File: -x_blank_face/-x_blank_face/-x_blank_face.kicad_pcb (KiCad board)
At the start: 2 copper layers, 87 x 326.5 mm, 29 parts, among them J1 Conn_01x08_Pin, J2 Conn_01x02_Pin, J3 Conn_01x02_Pin

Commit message: Rerouted some stuff
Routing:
- net GND: track 221.4 -> 216.8 mm
- net /-X Serial Out: track 219.9 -> 215.8 mm

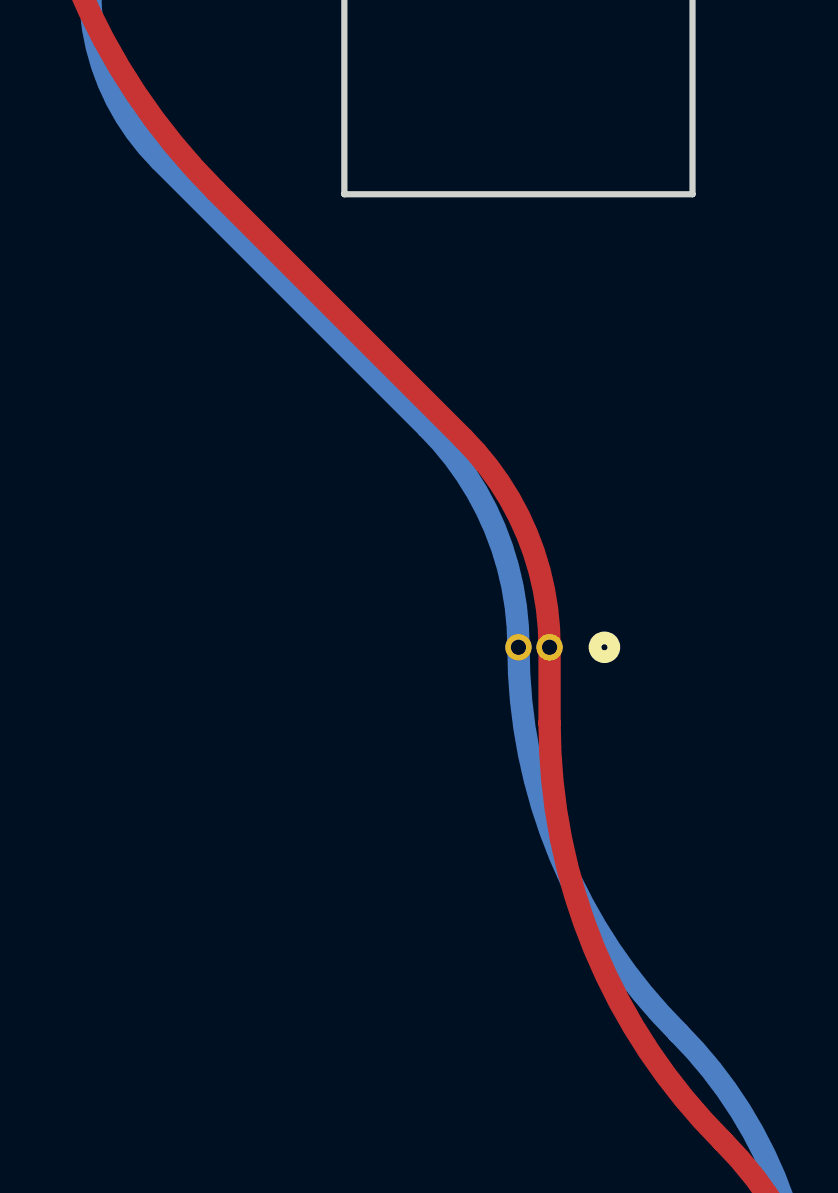
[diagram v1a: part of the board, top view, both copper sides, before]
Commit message: removed solder mask from footprint
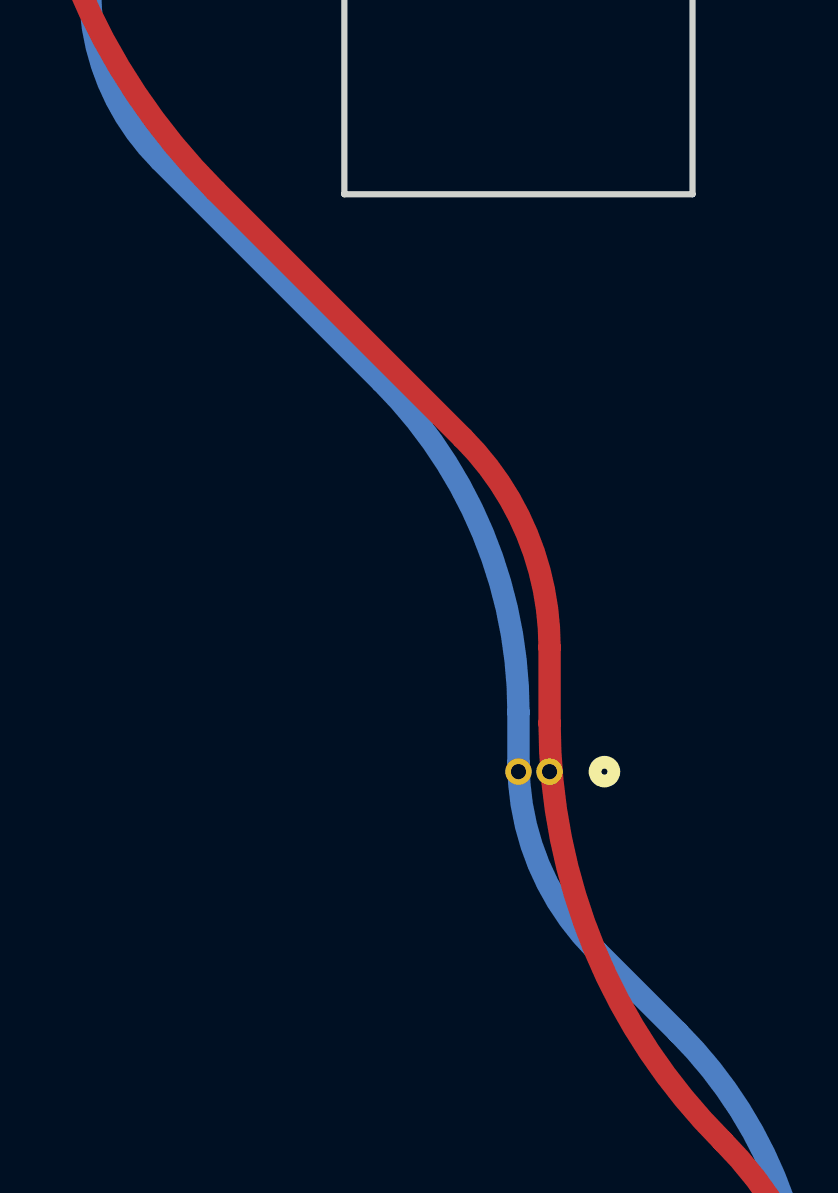
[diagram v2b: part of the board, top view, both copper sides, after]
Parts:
- moved J2 5.00 mm to (134.8, 25.6)
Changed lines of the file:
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@@
 	(footprint "CNN_GNSS_Footprint:CON2_1X2_UR_DF13"
 		(layer "B.Cu")
-		(at 134.7616 20.6161)
+		(at 134.7616 25.6161)
 		(tags "DF13-2P-1.25DS20 ")
 		(property "Reference" "J2"
@@
 	)
 	(segment
-		(start 134.7616 20.6316)
-		(end 134.7616 20.6161)
-		(width 0.2)
-		(layer "B.Cu")
-		(net 1)
-	)
-	(segment
 		(start 113.785 -38.15)
 		(end 113.785 -38.4)
@@
 	(segment
 		(start 119.113427 1.038427)
-		(end 129.849137 11.774137)
+		(end 128.00469 9.92969)
 		(width 0.9)
 		(layer "B.Cu")
@@
 	)
 	(segment
+		(start 139.925354 36.100354)
+		(end 136.634579 32.809581)
+		(width 0.9)
+		(layer "B.Cu")
+		(net 3)
+	)
+	(segment
 		(start 132.9516 158.6784)
 		(end 132.9516 163.3161)
+		(width 0.9)
+		(layer "B.Cu")
+		(net 3)
+	)
+	(segment
+		(start 133.511588 23.224603)
+		(end 133.511579 25.269945)
 		(width 0.9)
 		(layer "B.Cu")
@@
 	)
 	(arc
-		(start 133.5116 20.6161)
-		(mid 132.559757 15.830865)
-		(end 129.849137 11.774137)
-		(width 0.9)
-		(layer "B.Cu")
-		(net 3)
-	)
-	(arc
-		(start 139.925354 36.100354)
-		(mid 135.17848 28.996155)
-		(end 133.5116 20.6161)
+		(start 133.511588 23.224603)
+		(mid 132.080408 16.029448)
+		(end 128.00469 9.92969)
+		(width 0.9)
+		(layer "B.Cu")
+		(net 3)
+	)
+	(arc
+		(start 136.634579 32.809581)
+		(mid 134.323211 29.350367)
+		(end 133.511579 25.269945)
 		(width 0.9)
 		(layer "B.Cu")
@@
 		(name "$teardrop_padvia$")
 		(hatch none 0.1)
-		(priority 30001)
+		(priority 30000)
 		(attr
 			(teardrop
@@
 		(polygon
 			(pts
-				(xy 135.2116 21.672651) (xy 135.210513 21.464825) (xy 135.210208 21.282705) (xy 135.217725 21.131184)
-				(xy 135.240196 20.960319) (xy 135.284751 20.720161) (xy 134.7616 20.6151) (xy 134.238449 20.720161)
-				(xy 134.293314 21.027554) (xy 134.312002 21.239949) (xy 134.312686 21.46483) (xy 134.3116 21.672651)
+				(xy 133.7516 162.259549) (xy 133.752686 162.467369) (xy 133.752992 162.649492) (xy 133.745475 162.801013)
+				(xy 133.723004 162.97188) (xy 133.678449 163.212039) (xy 134.2016 163.3171) (xy 134.724751 163.212039)
+				(xy 134.669886 162.904651) (xy 134.651198 162.69226) (xy 134.650513 162.467374) (xy 134.6516 162.259549)
 			)
 		)
@@
 		(name "$teardrop_padvia$")
 		(hatch none 0.1)
-		(priority 30002)
+		(priority 30001)
 		(attr
 			(teardrop
@@
 		(polygon
 			(pts
-				(xy 133.7516 162.259549) (xy 133.752686 162.467369) (xy 133.752992 162.649492) (xy 133.745475 162.801013)
-				(xy 133.723004 162.97188) (xy 133.678449 163.212039) (xy 134.2016 163.3171) (xy 134.724751 163.212039)
-				(xy 134.669886 162.904651) (xy 134.651198 162.69226) (xy 134.650513 162.467374) (xy 134.6516 162.259549)
+				(xy 134.334996 24.673626) (xy 134.339231 24.907449) (xy 134.327891 25.069276) (xy 134.285379 25.290009)
+				(xy 134.238449 25.512039) (xy 134.761641 25.617099) (xy 135.284751 25.512039) (xy 135.251272 25.319208)
+				(xy 135.236773 25.177196) (xy 135.235978 24.978185) (xy 135.234226 24.636433)
 			)
 		)
 	)
 	(zone
-		(net 1)
-		(net_name "GND")
-		(layer "F.Cu")
+		(net 3)
+		(net_name "/-X Serial Out")
+		(layer "B.Cu")
 		(name "$teardrop_padvia$")
 		(hatch none 0.1)
@@
 		(polygon
 			(pts
-				(xy 134.268592 19.611032) (xy 134.274748 19.665481) (xy 134.299803 19.904922) (xy 134.304968 20.07816)
-				(xy 134.285948 20.256698) (xy 134.238449 20.512039) (xy 134.761711 20.617093) (xy 135.284751 20.512039)
-				(xy 135.236084 20.243147) (xy 135.211938 20.054674) (xy 135.199117 19.900902) (xy 135.162932 19.510267)
+				(xy 134.0522 26.615048) (xy 134.038229 26.461726) (xy 134.035257 26.335368) (xy 134.052009 26.115686)
+				(xy 134.055467 26.088274) (xy 134.068286 25.975693) (xy 134.073703 25.852121) (xy 134.064823 25.702566)
+				(xy 134.034751 25.512039) (xy 133.51148 25.615108) (xy 132.988449 25.720161) (xy 133.036775 25.959712)
+				(xy 133.100411 26.292816) (xy 133.158763 26.723526)
 			)
 		)
@@
 		(name "$teardrop_padvia$")
 		(hatch none 0.1)
-		(priority 30000)
+		(priority 30001)
 		(attr
 			(teardrop
@@
 		(polygon
 			(pts
-				(xy 133.022265 19.610793) (xy 133.024859 19.633806) (xy 133.051574 19.889468) (xy 133.057068 20.069557)
-				(xy 133.037355 20.251329) (xy 132.988449 20.512039) (xy 133.511711 20.617093) (xy 134.034751 20.512039)
-				(xy 133.98826 20.25424) (xy 133.965107 20.071844) (xy 133.952435 19.910818) (xy 133.916605 19.510026)
+				(xy 132.5016 162.259549) (xy 132.502686 162.467369) (xy 132.502992 162.649492) (xy 132.495475 162.801013)
+				(xy 132.473004 162.97188) (xy 132.428449 163.212039) (xy 132.9516 163.3171) (xy 133.474751 163.212039)
+				(xy 133.419886 162.904651) (xy 133.401198 162.69226) (xy 133.400513 162.467374) (xy 133.4016 162.259549)
+			)
+		)
+	)
+	(zone
+		(net 2)
+		(net_name "/+X Drain")
+		(layer "B.Cu")
+		(hatch edge 0.5)
+		(connect_pads
+			(clearance 0.5)
+		)
+		(min_thickness 0.25)
+		(filled_areas_thickness no)
+		(fill yes
+			(thermal_gap 0.5)
+			(thermal_bridge_width 0.5)
+		)
+		(polygon
+			(pts
+				(xy 68.458065 -44.722627) (xy 155.701705 -44.722627) (xy 155.707104 131.687373) (xy 68.452666 131.687373)
 			)
 		)
@@
 		(name "$teardrop_padvia$")
 		(hatch none 0.1)
-		(priority 30001)
+		(priority 30002)
 		(attr
 			(teardrop
@@
 		(polygon
 			(pts
-				(xy 132.5016 162.259549) (xy 132.502686 162.467369) (xy 132.502992 162.649492) (xy 132.495475 162.801013)
-				(xy 132.473004 162.97188) (xy 132.428449 163.212039) (xy 132.9516 163.3171) (xy 133.474751 163.212039)
-				(xy 133.419886 162.904651) (xy 133.401198 162.69226) (xy 133.400513 162.467374) (xy 133.4016 162.259549)
-			)
-		)
-	)
-	(zone
-		(net 3)
-		(net_name "/-X Serial Out")
-		(layer "B.Cu")
-		(name "$teardrop_padvia$")
-		(hatch none 0.1)
-		(priority 30002)
-		(attr
-			(teardrop
-				(type padvia)
-			)
-		)
-		(connect_pads yes
-			(clearance 0)
-		)
-		(min_thickness 0.0254)
-		(filled_areas_thickness no)
-		(fill yes
-			(thermal_gap 0.5)
-			(thermal_bridge_width 0.5)
-			(island_removal_mode 1)
-			(island_area_min 10)
-		)
-		(polygon
-			(pts
-				(xy 133.9826 21.512527) (xy 133.978679 21.420547) (xy 133.97182 21.23115) (xy 133.975089 21.08847)
-				(xy 133.994171 20.936731) (xy 134.034751 20.720161) (xy 133.511559 20.615101) (xy 132.988449 20.720161)
-				(xy 133.057962 21.114329) (xy 133.080616 21.482523) (xy 133.08337 21.549715)
-			)
-		)
-	)
-	(zone
-		(net 2)
-		(net_name "/+X Drain")
-		(layer "B.Cu")
-		(hatch edge 0.5)
-		(connect_pads
-			(clearance 0.5)
-		)
-		(min_thickness 0.25)
-		(filled_areas_thickness no)
-		(fill yes
-			(thermal_gap 0.5)
-			(thermal_bridge_width 0.5)
-		)
-		(polygon
-			(pts
-				(xy 68.458065 -44.722627) (xy 155.701705 -44.722627) (xy 155.707104 131.687373) (xy 68.452666 131.687373)
-			)
-		)
+				(xy 133.061583 24.559548) (xy 133.062671 24.767507) (xy 133.062978 24.949568) (xy 133.055463 25.101062)
+				(xy 133.032996 25.271911) (xy 132.988449 25.512039) (xy 133.5116 25.617099) (xy 134.034751 25.512039)
+				(xy 133.979865 25.204532) (xy 133.96118 24.992055) (xy 133.960497 24.767231) (xy 133.961582 24.559551)
+			)
+		)

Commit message: reviewed boards
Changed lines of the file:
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@@
 			(at 6.181 0.07 180)
 			(layer "F.SilkS")
+			(hide yes)
 			(effects
 				(font
@@
 			(at 6.221 0.04 180)
 			(layer "F.SilkS")
+			(hide yes)
 			(effects
 				(font
@@
 			(at 6.231 0.04 180)
 			(layer "F.SilkS")
+			(hide yes)
 			(effects
 				(font
@@
 			(at 6.251 -0.03 180)
 			(layer "F.SilkS")
+			(hide yes)
 			(effects
 				(font
@@
 		(name "$teardrop_padvia$")
 		(hatch none 0.1)
-		(priority 30000)
+		(priority 30001)
 		(attr
 			(teardrop
@@
 		(polygon
 			(pts
-				(xy 134.0522 26.615048) (xy 134.038229 26.461726) (xy 134.035257 26.335368) (xy 134.052009 26.115686)
-				(xy 134.055467 26.088274) (xy 134.068286 25.975693) (xy 134.073703 25.852121) (xy 134.064823 25.702566)
-				(xy 134.034751 25.512039) (xy 133.51148 25.615108) (xy 132.988449 25.720161) (xy 133.036775 25.959712)
-				(xy 133.100411 26.292816) (xy 133.158763 26.723526)
+				(xy 132.5016 162.259549) (xy 132.502686 162.467369) (xy 132.502992 162.649492) (xy 132.495475 162.801013)
+				(xy 132.473004 162.97188) (xy 132.428449 163.212039) (xy 132.9516 163.3171) (xy 133.474751 163.212039)
+				(xy 133.419886 162.904651) (xy 133.401198 162.69226) (xy 133.400513 162.467374) (xy 133.4016 162.259549)
 			)
 		)
@@
 		(name "$teardrop_padvia$")
 		(hatch none 0.1)
-		(priority 30001)
+		(priority 30002)
 		(attr
 			(teardrop
@@
 		(polygon
 			(pts
-				(xy 132.5016 162.259549) (xy 132.502686 162.467369) (xy 132.502992 162.649492) (xy 132.495475 162.801013)
-				(xy 132.473004 162.97188) (xy 132.428449 163.212039) (xy 132.9516 163.3171) (xy 133.474751 163.212039)
-				(xy 133.419886 162.904651) (xy 133.401198 162.69226) (xy 133.400513 162.467374) (xy 133.4016 162.259549)
-			)
-		)
-	)
-	(zone
-		(net 2)
-		(net_name "/+X Drain")
-		(layer "B.Cu")
-		(hatch edge 0.5)
-		(connect_pads
-			(clearance 0.5)
-		)
-		(min_thickness 0.25)
-		(filled_areas_thickness no)
-		(fill yes
-			(thermal_gap 0.5)
-			(thermal_bridge_width 0.5)
-		)
-		(polygon
-			(pts
-				(xy 68.458065 -44.722627) (xy 155.701705 -44.722627) (xy 155.707104 131.687373) (xy 68.452666 131.687373)
+				(xy 133.061583 24.559548) (xy 133.062671 24.767507) (xy 133.062978 24.949568) (xy 133.055463 25.101062)
+				(xy 133.032996 25.271911) (xy 132.988449 25.512039) (xy 133.5116 25.617099) (xy 134.034751 25.512039)
+				(xy 133.979865 25.204532) (xy 133.96118 24.992055) (xy 133.960497 24.767231) (xy 133.961582 24.559551)
 			)
 		)
@@
 		(name "$teardrop_padvia$")
 		(hatch none 0.1)
-		(priority 30002)
+		(priority 30000)
 		(attr
 			(teardrop
@@
 		(polygon
 			(pts
-				(xy 133.061583 24.559548) (xy 133.062671 24.767507) (xy 133.062978 24.949568) (xy 133.055463 25.101062)
-				(xy 133.032996 25.271911) (xy 132.988449 25.512039) (xy 133.5116 25.617099) (xy 134.034751 25.512039)
-				(xy 133.979865 25.204532) (xy 133.96118 24.992055) (xy 133.960497 24.767231) (xy 133.961582 24.559551)
+				(xy 134.0522 26.615048) (xy 134.038229 26.461726) (xy 134.035257 26.335368) (xy 134.052009 26.115686)
+				(xy 134.055467 26.088274) (xy 134.068286 25.975693) (xy 134.073703 25.852121) (xy 134.064823 25.702566)
+				(xy 134.034751 25.512039) (xy 133.51148 25.615108) (xy 132.988449 25.720161) (xy 133.036775 25.959712)
+				(xy 133.100411 26.292816) (xy 133.158763 26.723526)
+			)
+		)
+	)
+	(zone
+		(net 2)
+		(net_name "/+X Drain")
+		(layer "B.Cu")
+		(hatch edge 0.5)
+		(connect_pads
+			(clearance 0.5)
+		)
+		(min_thickness 0.25)
+		(filled_areas_thickness no)
+		(fill yes
+			(thermal_gap 0.5)
+			(thermal_bridge_width 0.5)
+		)
+		(polygon
+			(pts
+				(xy 68.458065 -44.722627) (xy 155.701705 -44.722627) (xy 155.707104 131.687373) (xy 68.452666 131.687373)
 			)
 		)

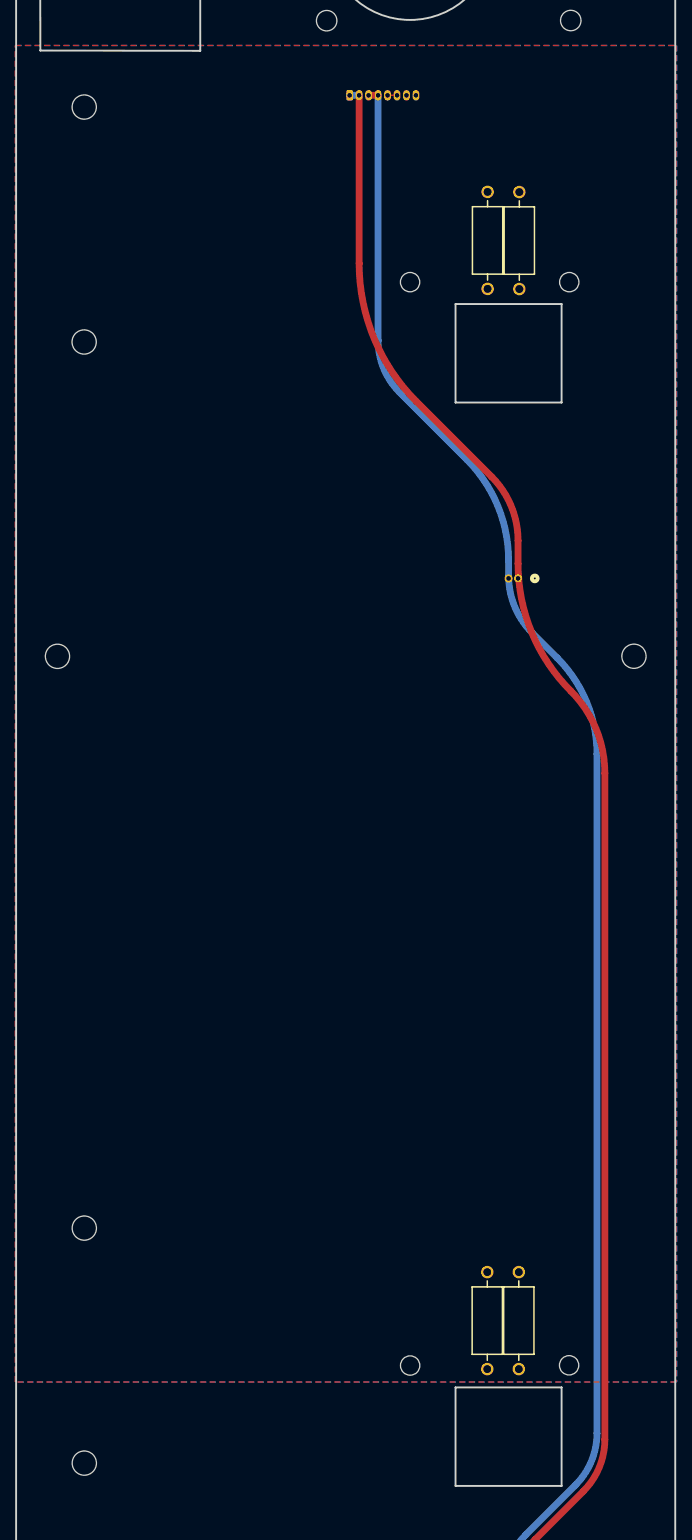
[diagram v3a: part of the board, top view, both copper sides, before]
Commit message: Removed GND and PWR plane, replaced with traces, switches are now in series rather than in parallel
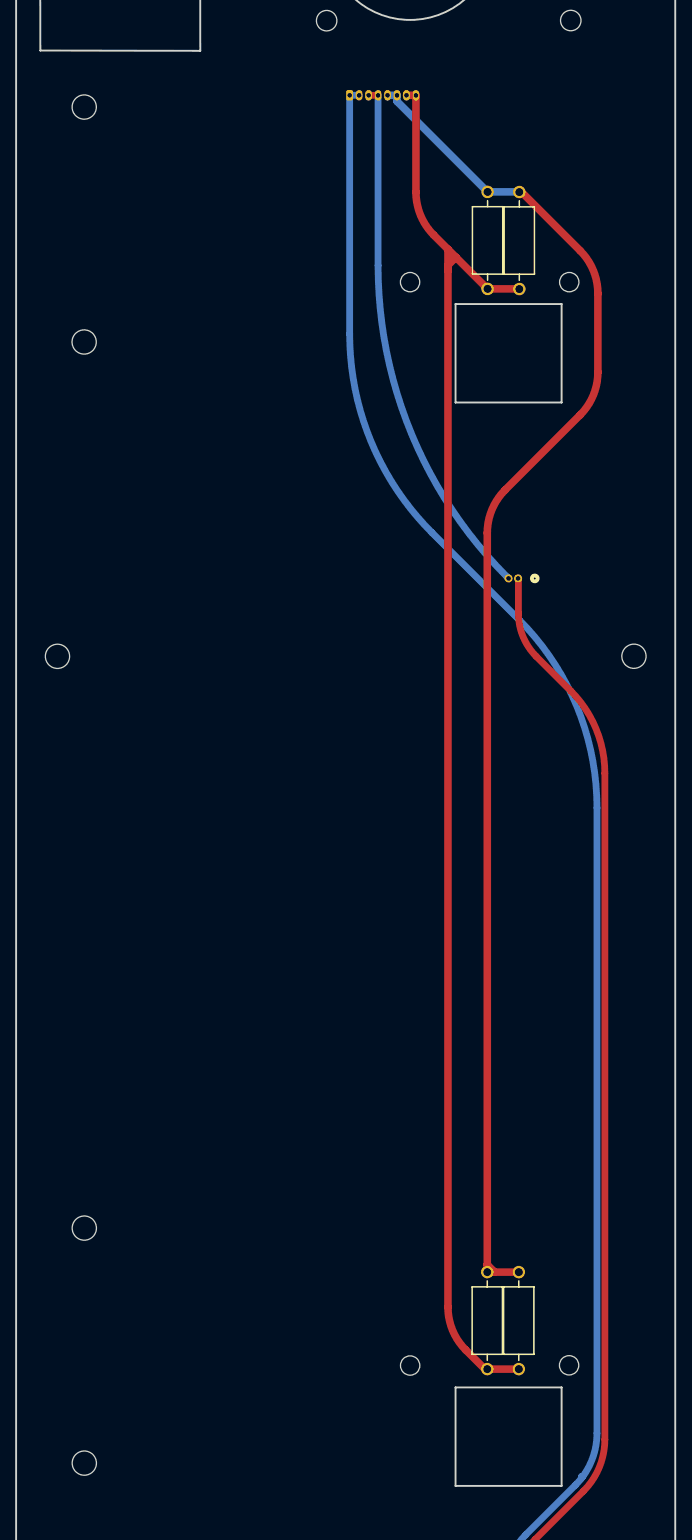
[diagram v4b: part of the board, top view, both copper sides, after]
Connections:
- J2 pad 1: GND -> Net-(J2-Pin_1)
- J3 pad 1: GND -> Net-(J2-Pin_1)
- J3 pad 2: /-X Serial Out -> GND
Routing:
- net /12VPDM: track 0.00 -> 190.7 mm
- net /+X Drain: track 1.89 -> 181.2 mm
- net /-X Serial Out: track 216.1 -> 69.4 mm
- net Net-(J2-Pin_1): track 0.00 -> 145.4 mm
- net GND: track 216.7 -> 217.5 mm
- removed copper zone on B.Cu, net /+X Drain
- removed copper zone on F.Cu, net /12VPDM

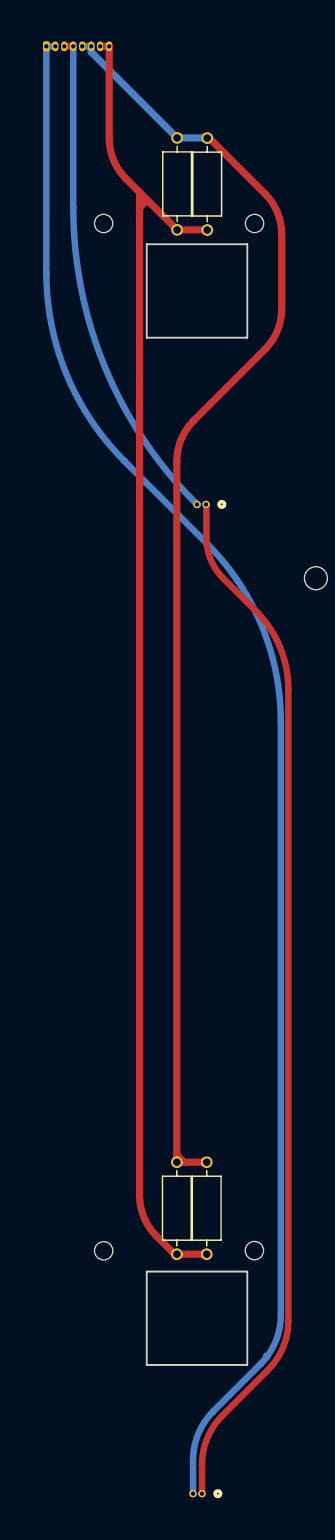
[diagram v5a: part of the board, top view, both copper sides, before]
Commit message: changed cover panels to have smaller power planes, also changed front panel DF13 from SMD to THT
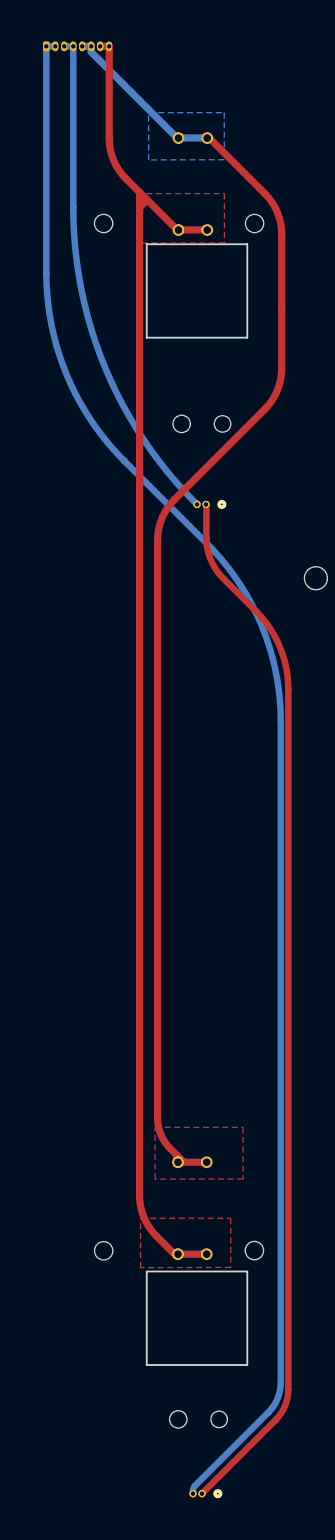
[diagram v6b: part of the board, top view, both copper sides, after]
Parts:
- moved R2 0.19 mm to (130.9, -12.6)
- moved R3 0.16 mm to (130.9, 130.0)
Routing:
- net /+X Drain: track 181.2 -> 183.1 mm
- net Net-(J2-Pin_1): track 145.4 -> 146.0 mm
- added copper zone on B.Cu, net /+X Drain
- added copper zone on F.Cu, net /+X Drain
- added copper zone on F.Cu, net /12VPDM
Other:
- outline, holes or cut-outs redrawn
